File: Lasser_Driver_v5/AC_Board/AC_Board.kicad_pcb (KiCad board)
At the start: 2 copper layers, 62.4 x 42.7 mm, 9 parts, among them J1 Screw_Terminal_01x03, J2 Screw_Terminal_01x03, J3 Screw_Terminal_01x03

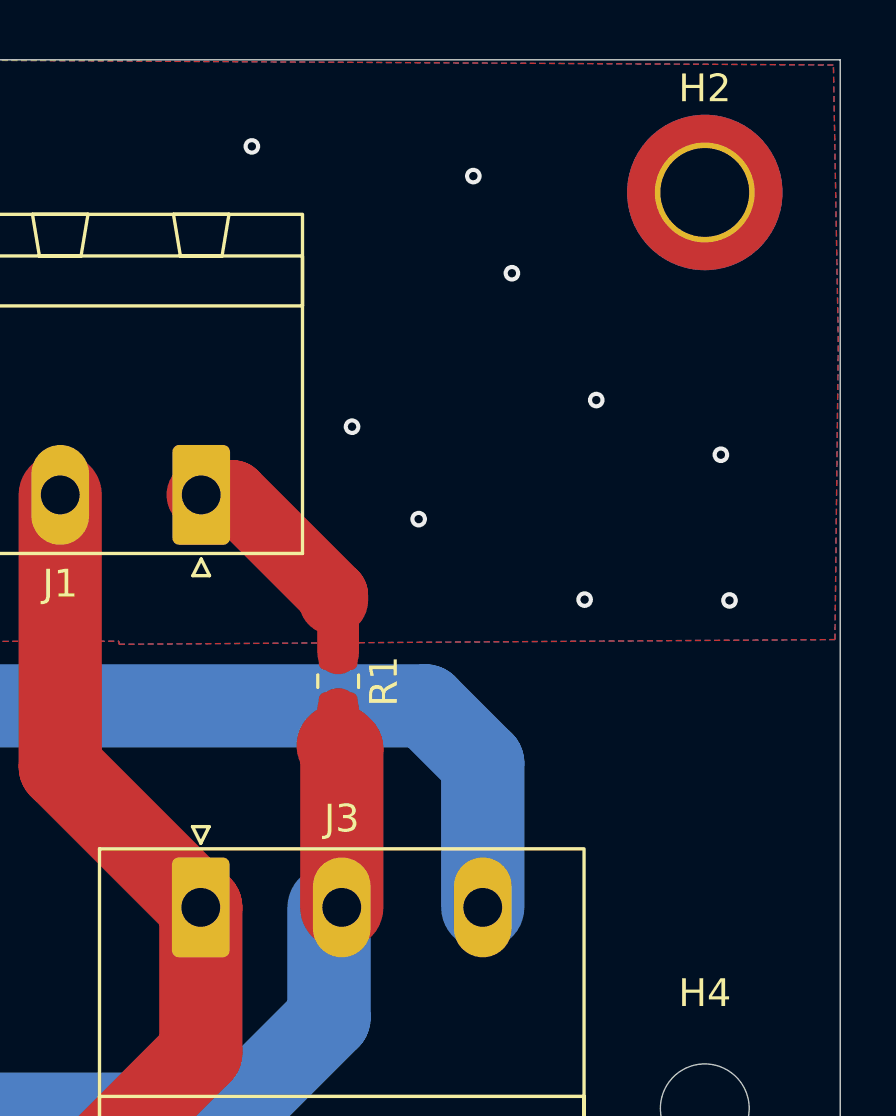
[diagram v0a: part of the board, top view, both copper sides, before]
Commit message: v5 ac board and pm22V board ready
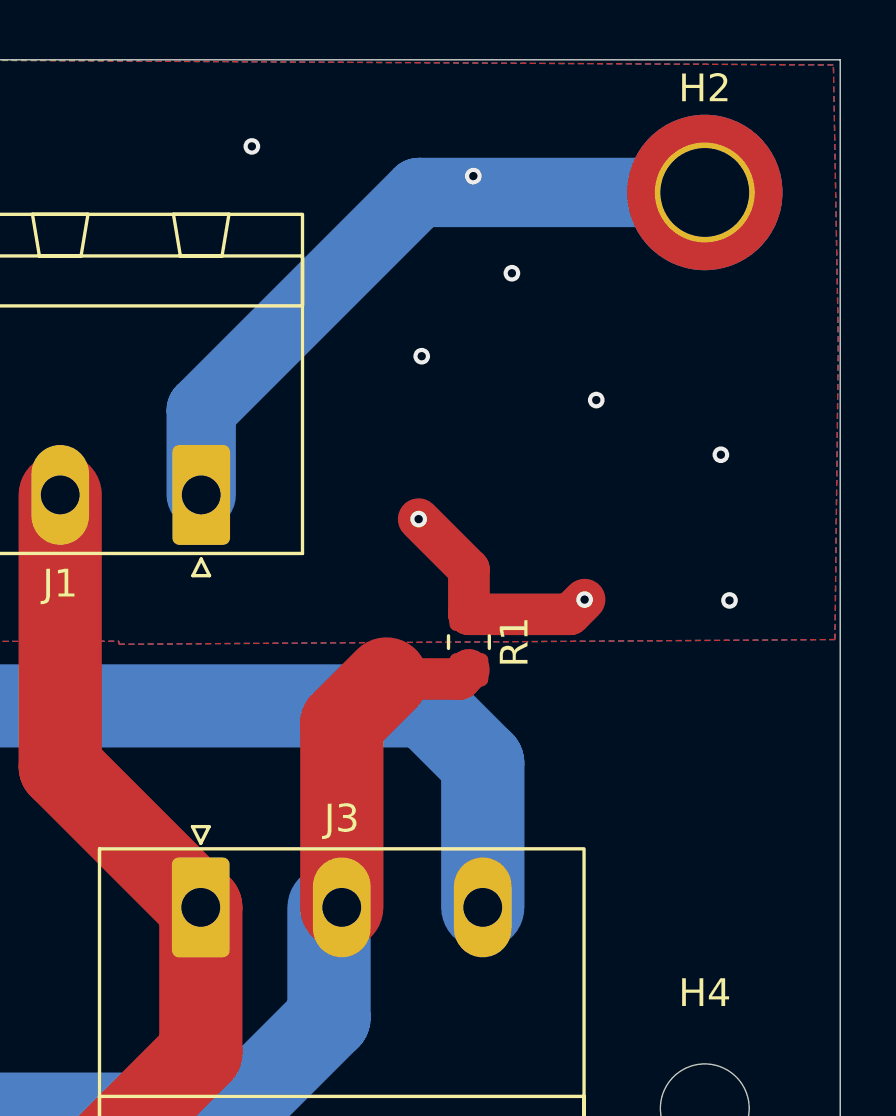
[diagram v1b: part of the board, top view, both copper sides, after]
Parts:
- moved R1 4.92 mm to (97.5, 56.2)
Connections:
- net 0Vac renamed Neutral
- net Net-(J2-Pin_3) renamed /Line_TH
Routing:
- net Earth: track 8.87 -> 33.0 mm
- net Net-(J2-Pin_2): track 43.8 -> 48.6 mm
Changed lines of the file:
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@@
 			(layers "*.Cu" "*.Mask")
 			(remove_unused_layers no)
-			(net "Net-(J2-Pin_3)")
+			(net "/Line_TH")
 			(pintype "passive")
 		)
@@
 	(footprint "Resistor_SMD:R_0805_2012Metric_Pad1.20x1.40mm_HandSolder"
 		(layer "F.Cu")
-		(at 92.79 57.61 -90)
+		(at 97.5 56.2 -90)
 		(descr "Resistor SMD 0805 (2012 Metric), square (rectangular) end terminal, IPC-7351 nominal with elongated pad for handsoldering. (Body size source: IPC-SM-782 page 72, https://www.pcb-3d.com/wordpress/wp-content/uploads/ipc-sm-782a_amendment_1_and_2.pdf)")
 		(tags "resistor handsolder")
@@
 			(layers "*.Cu" "*.Mask")
 			(remove_unused_layers no)
-			(net "0Vac")
+			(net "Neutral")
 			(pinfunction "Pin_2_2")
 			(pintype "passive")
@@
 			(remove_unused_layers no)
 			(roundrect_rratio 0.120192)
-			(net "0Vac")
+			(net "Neutral")
 			(pinfunction "Pin_1_1")
 			(pintype "passive")
@@
 			(layers "*.Cu" "*.Mask")
 			(remove_unused_layers no)
-			(net "Net-(J2-Pin_3)")
+			(net "/Line_TH")
 			(pinfunction "Pin_3_3")
 			(pintype "passive")
@@
 			(remove_unused_layers no)
 			(roundrect_rratio 0.120192)
-			(net "0Vac")
+			(net "Neutral")
 			(pinfunction "Pin_1_1")
 			(pintype "passive")
@@
 			(layers "*.Cu" "*.Mask")
 			(remove_unused_layers no)
-			(net "Net-(J2-Pin_3)")
+			(net "/Line_TH")
 			(pinfunction "Pin_3_3")
 			(pintype "passive")
@@
 	)
 	(segment
-		(start 98 65.76)
-		(end 98 60.56)
-		(width 3)
-		(layer "B.Cu")
-		(net "Net-(J2-Pin_3)")
-	)
-	(segment
-		(start 70.01 58.51)
-		(end 70.02 58.5)
-		(width 3)
-		(layer "B.Cu")
-		(net "Net-(J2-Pin_3)")
-	)
-	(segment
-		(start 71.605 60.105)
-		(end 70.01 58.51)
-		(width 3)
-		(layer "B.Cu")
-		(net "Net-(J2-Pin_3)")
-	)
-	(segment
-		(start 70.02 58.5)
-		(end 95.94 58.5)
-		(width 3)
-		(layer "B.Cu")
-		(net "Net-(J2-Pin_3)")
-	)
-	(segment
-		(start 71.605 65.5925)
-		(end 71.605 60.105)
-		(width 3)
-		(layer "B.Cu")
-		(net "Net-(J2-Pin_3)")
-	)
-	(segment
-		(start 98 60.56)
-		(end 95.94 58.5)
-		(width 3)
-		(layer "B.Cu")
-		(net "Net-(J2-Pin_3)")
-	)
-	(segment
-		(start 89.0025 50.8975)
-		(end 92.62 54.515)
-		(width 2.5)
-		(layer "F.Cu")
-		(net "Earth")
-	)
-	(segment
-		(start 92.79 54.43)
-		(end 92.62 54.26)
+		(start 97.5 55.2)
+		(end 101.14 55.2)
 		(width 1.5)
 		(layer "F.Cu")
@@
 	)
 	(segment
-		(start 92.79 56.61)
-		(end 92.79 54.43)
+		(start 97.5 53.58)
+		(end 95.69 51.77)
 		(width 1.5)
 		(layer "F.Cu")
@@
 	)
 	(segment
-		(start 87.855 50.8975)
-		(end 89.0025 50.8975)
-		(width 2.5)
-		(layer "F.Cu")
-		(net "Earth")
-	)
-	(segment
-		(start 92.62 54.515)
-		(end 92.62 54.7)
-		(width 2.5)
+		(start 97.5 55.2)
+		(end 97.5 53.58)
+		(width 1.5)
+		(layer "F.Cu")
+		(net "Earth")
+	)
+	(segment
+		(start 101.14 55.2)
+		(end 101.67 54.67)
+		(width 1.5)
 		(layer "F.Cu")
 		(net "Earth")
@@
 	)
 	(via
-		(at 93.29 48.44)
+		(at 95.8 45.9)
 		(size 0.6)
 		(drill 0.3)
@@
 	)
 	(segment
-		(start 92.92 60.06)
-		(end 92.79 59.93)
-		(width 3)
+		(start 87.855 50.8975)
+		(end 87.855 47.845)
+		(width 2.5)
+		(layer "B.Cu")
+		(net "Earth")
+	)
+	(segment
+		(start 95.7 40)
+		(end 106 40)
+		(width 2.5)
+		(layer "B.Cu")
+		(net "Earth")
+	)
+	(segment
+		(start 87.855 47.845)
+		(end 95.7 40)
+		(width 2.5)
+		(layer "B.Cu")
+		(net "Earth")
+	)
+	(segment
+		(start 97.170209 57.529791)
+		(end 97.5 57.2)
+		(width 1.5)
 		(layer "F.Cu")
 		(net "Net-(J2-Pin_2)")
 	)
 	(segment
+		(start 94.529791 57.529791)
+		(end 97.170209 57.529791)
+		(width 1.5)
+		(layer "F.Cu")
+		(net "Net-(J2-Pin_2)")
+	)
+	(segment
+		(start 92.92 59.139582)
+		(end 94.529791 57.529791)
+		(width 3)
+		(layer "F.Cu")
+		(net "Net-(J2-Pin_2)")
+	)
+	(segment
 		(start 92.92 65.76)
-		(end 92.92 60.06)
-		(width 3)
-		(layer "F.Cu")
-		(net "Net-(J2-Pin_2)")
-	)
-	(segment
-		(start 92.79 58.61)
-		(end 92.79 59.93)
-		(width 1.5)
+		(end 92.92 59.139582)
+		(width 3)
 		(layer "F.Cu")
 		(net "Net-(J2-Pin_2)")
@@
 		(width 3)
 		(layer "F.Cu")
-		(net "0Vac")
+		(net "Neutral")
 	)
 	(segment
@@
 		(width 3)
 		(layer "F.Cu")
-		(net "0Vac")
+		(net "Neutral")
 	)
 	(segment
@@
 		(width 3)
 		(layer "F.Cu")
-		(net "0Vac")
+		(net "Neutral")
 	)
 	(segment
@@
 		(width 3)
 		(layer "F.Cu")
-		(net "0Vac")
+		(net "Neutral")
 	)
 	(segment
@@
 		(width 3)
 		(layer "F.Cu")
-		(net "0Vac")
+		(net "Neutral")
 	)
 	(segment
@@
 		(width 3)
 		(layer "F.Cu")
-		(net "0Vac")
+		(net "Neutral")
 	)
 	(segment
@@
 		(width 3)
 		(layer "F.Cu")
-		(net "0Vac")
+		(net "Neutral")
+	)
+	(segment
+		(start 98 65.76)
+		(end 98 60.56)
+		(width 3)
+		(layer "B.Cu")
+		(net "/Line_TH")
+	)
+	(segment
+		(start 70.01 58.51)
+		(end 70.02 58.5)
+		(width 3)
+		(layer "B.Cu")
+		(net "/Line_TH")
+	)
+	(segment
+		(start 71.605 60.105)
+		(end 70.01 58.51)
+		(width 3)
+		(layer "B.Cu")
+		(net "/Line_TH")
+	)
+	(segment
+		(start 70.02 58.5)
+		(end 95.94 58.5)
+		(width 3)
+		(layer "B.Cu")
+		(net "/Line_TH")
+	)
+	(segment
+		(start 71.605 65.5925)
+		(end 71.605 60.105)
+		(width 3)
+		(layer "B.Cu")
+		(net "/Line_TH")
+	)
+	(segment
+		(start 98 60.56)
+		(end 95.94 58.5)
+		(width 3)
+		(layer "B.Cu")
+		(net "/Line_TH")
 	)
 	(zone
